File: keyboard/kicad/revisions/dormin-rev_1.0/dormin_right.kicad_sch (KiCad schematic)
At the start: 103 parts, among them J6_R1 Conn_01x04, Q3_R1 AO3407A, Q4_R1 AO3400A, SW21 SW_Push, SW22 SW_Push, SW23 SW_Push, SW24 SW_Push, SW25 SW_Push, SW26 SW_Push, SW27 SW_Push, SW28 SW_Push, SW29 SW_Push, SW30 SW_Push, SW31 SW_Push, SW32 SW_Push, SW33 SW_Push, SW34 SW_Push, SW35 SW_Push, SW36 SW_Push, SW37 SW_Push, SW38 SW_Push, SW39 SW_Push, SW40 SW_Push, U1 XIAO-nRF52840-SMD

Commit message: chore: added temporary routing
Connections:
- net VBAT_R: now also TP4_R1.1
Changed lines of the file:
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@@
+	)
+	(junction
+		(at 68.58 83.82)
+		(diameter 0)
+		(color 0 0 0 0)
 	)
 	(junction
@@
 	(wire
 		(pts
-			(xy 68.58 81.28) (xy 68.58 90.17)
+			(xy 68.58 81.28) (xy 68.58 83.82)
 		)
 		(stroke
@@
 	(wire
 		(pts
+			(xy 62.23 83.82) (xy 68.58 83.82)
+		)
+		(stroke
+			(width 0)
+			(type default)
+		)
+	)
+	(wire
+		(pts
 			(xy 207.01 148.59) (xy 213.36 148.59)
 		)
@@
 		)
 		(stroke
+			(width 0)
+			(type default)
+		)
+	)
+	(wire
+		(pts
+			(xy 68.58 83.82) (xy 68.58 90.17)
+		)
+		(stroke

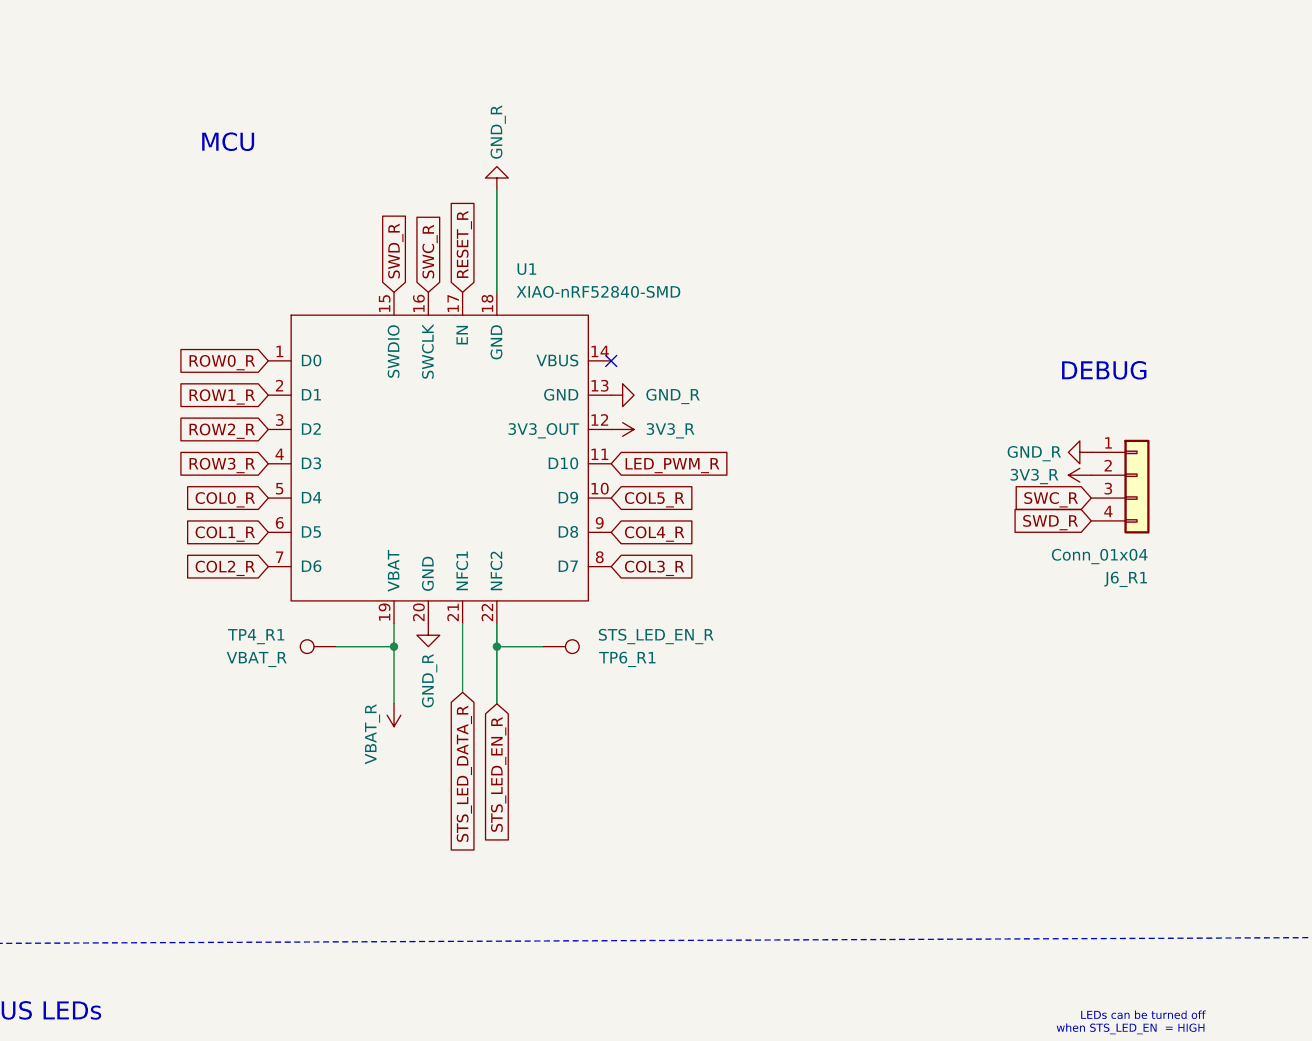
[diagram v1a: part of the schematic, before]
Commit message: chore: finish main routing
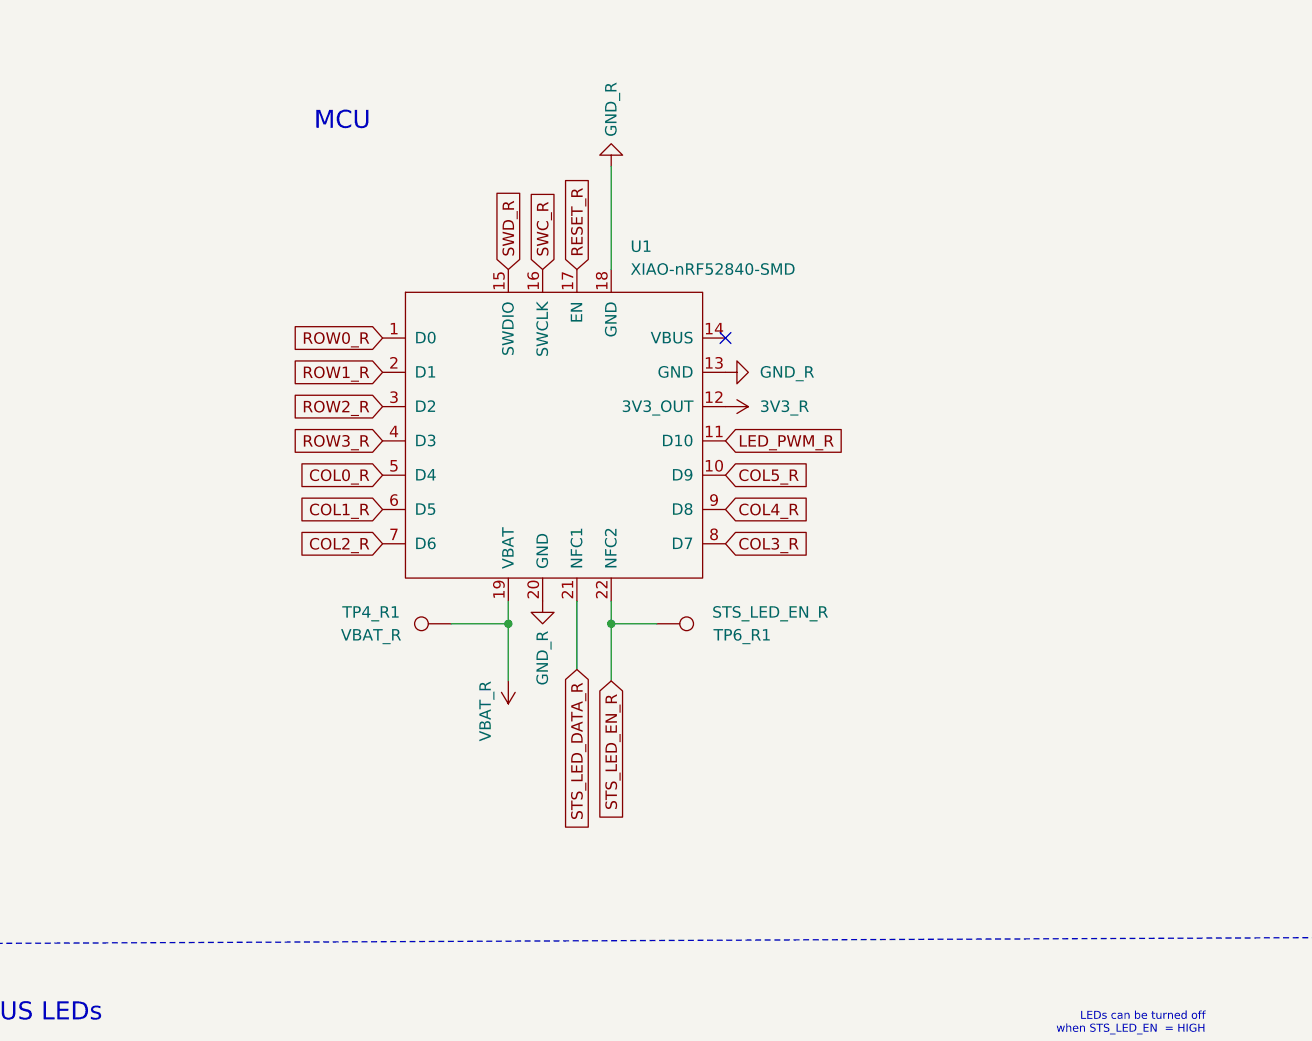
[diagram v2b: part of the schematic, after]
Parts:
- removed J6_R1: Conn_01x04, Connector_PinSocket_2.54mm:PinSocket_1x04_P2.54mm_Vertical, symbol Connector_Generic:Conn_01x04
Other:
- note removed: "DEBUG"
- moved on the sheet: TP4_R1, TP6_R1, U1
